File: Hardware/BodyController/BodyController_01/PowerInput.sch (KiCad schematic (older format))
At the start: 39 parts, among them Q1 NX1029X,115, Q2 NX1029X,115, Q4 SQJ423EP-T1_GE3, U14 OPA320-Q1, U2 LM2903QDRQ1, U3 INA21x

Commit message: New bring-up code for Body Controller
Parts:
- C16, C17, C18, C20, C21, C79: MPN CGA4J3X7R1H105K125AE -> CGA4J3X7R1H105M125AE
- D8: MPN MMSZ4702T1G -> MMSZ5245BT1G
- R14, R15: value 10R -> 3R0; MPN AC0603FR-0710RL -> ERJ-3GEYJ3R0V
- U2: MPN LM2903QDRQ1 -> LM2903AVQPWRG4Q1
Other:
- note added: "27A efuse\n20A/V\nOffset at 1.65V"
- note added: "Gain: 100V/V"
- note removed: "71A efuse\n25A/V\nOffset at 1.65V"
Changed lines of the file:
@@
-$EndComp
-$Comp
-L R R14
-U 1 1 599A2E3C
-P 6850 4550
-F 0 "R14" V 6930 4550 50  0000 C CNN
-F 1 "10R" V 6850 4550 50  0000 C CNN
-F 2 "Resistors_SMD:R_0603" V 6780 4550 50  0001 C CNN
-F 3 "http://www.yageo.com/NewPortal/yageodocoutput?fileName=/pdf/R-Chip/PYu-AC_51_RoHS_L_6.pdf" H 6850 4550 50  0001 C CNN
-F 4 "AC0603FR-0710RL" H 6930 4650 50  0001 C CNN "MPN"
-F 5 "y" H 6930 4650 50  0001 C CNN "populate"
-	1    6850 4550
-	0    1    1    0
-$EndComp
-$Comp
-L R R15
-U 1 1 599A2EC8
-P 6850 4950
-F 0 "R15" V 6930 4950 50  0000 C CNN
-F 1 "10R" V 6850 4950 50  0000 C CNN
-F 2 "Resistors_SMD:R_0603" V 6780 4950 50  0001 C CNN
-F 3 "http://www.yageo.com/NewPortal/yageodocoutput?fileName=/pdf/R-Chip/PYu-AC_51_RoHS_L_6.pdf" H 6850 4950 50  0001 C CNN
-F 4 "AC0603FR-0710RL" H 6930 5050 50  0001 C CNN "MPN"
-F 5 "y" H 6930 5050 50  0001 C CNN "populate"
-	1    6850 4950
-	0    1    1    0
 $EndComp
 $Comp
@@
 F 1 "1uF" H 6675 4250 50  0000 L CNN
 F 2 "Capacitors_SMD:C_0805" H 6688 4200 50  0001 C CNN
-F 3 "https://product.tdk.com/info/en/documents/chara_sheet/CGA4J3X7R1H105K125AE.pdf" H 6650 4350 50  0001 C CNN
-F 4 "CGA4J3X7R1H105K125AE" H 6675 4550 50  0001 C CNN "MPN"
+F 3 "https://product.tdk.com/info/en/documents/chara_sheet/CGA4J3X7R1H105M125AE.pdf" H 6650 4350 50  0001 C CNN
+F 4 "CGA4J3X7R1H105M125AE" H 6675 4550 50  0001 C CNN "MPN"
 F 5 "y" H 6675 4550 50  0001 C CNN "populate"
 	1    6650 4350
@@
 L GND #PWR023
 U 1 1 599A3E31
-P 6650 5350
-F 0 "#PWR023" H 6650 5100 50  0001 C CNN
-F 1 "GND" H 6650 5200 50  0000 C CNN
-F 2 "" H 6650 5350 50  0001 C CNN
-F 3 "" H 6650 5350 50  0001 C CNN
-	1    6650 5350
+P 6650 5450
+F 0 "#PWR023" H 6650 5200 50  0001 C CNN
+F 1 "GND" H 6650 5300 50  0000 C CNN
+F 2 "" H 6650 5450 50  0001 C CNN
+F 3 "" H 6650 5450 50  0001 C CNN
+	1    6650 5450
 	1    0    0    -1
 $EndComp
@@
 L C C18
 U 1 1 599A3E37
-P 6650 5150
-F 0 "C18" H 6675 5250 50  0000 L CNN
-F 1 "1uF" H 6675 5050 50  0000 L CNN
-F 2 "Capacitors_SMD:C_0805" H 6688 5000 50  0001 C CNN
-F 3 "https://product.tdk.com/info/en/documents/chara_sheet/CGA4J3X7R1H105K125AE.pdf" H 6650 5150 50  0001 C CNN
-F 4 "CGA4J3X7R1H105K125AE" H 6675 5350 50  0001 C CNN "MPN"
-F 5 "y" H 6675 5350 50  0001 C CNN "populate"
-	1    6650 5150
+P 6650 5250
+F 0 "C18" H 6675 5350 50  0000 L CNN
+F 1 "1uF" H 6675 5150 50  0000 L CNN
+F 2 "Capacitors_SMD:C_0805" H 6688 5100 50  0001 C CNN
+F 3 "https://product.tdk.com/info/en/documents/chara_sheet/CGA4J3X7R1H105M125AE.pdf" H 6650 5250 50  0001 C CNN
+F 4 "CGA4J3X7R1H105M125AE" H 6675 5450 50  0001 C CNN "MPN"
+F 5 "y" H 6675 5450 50  0001 C CNN "populate"
+	1    6650 5250
 	1    0    0    -1
 $EndComp
@@
 F 1 "1uF" H 6575 4650 50  0000 L CNN
 F 2 "Capacitors_SMD:C_0805" H 6588 4600 50  0001 C CNN
-F 3 "https://product.tdk.com/info/en/documents/chara_sheet/CGA4J3X7R1H105K125AE.pdf" H 6550 4750 50  0001 C CNN
-F 4 "CGA4J3X7R1H105K125AE" H 6575 4950 50  0001 C CNN "MPN"
+F 3 "https://product.tdk.com/info/en/documents/chara_sheet/CGA4J3X7R1H105M125AE.pdf" H 6550 4750 50  0001 C CNN
+F 4 "CGA4J3X7R1H105M125AE" H 6575 4950 50  0001 C CNN "MPN"
 F 5 "y" H 6575 4950 50  0001 C CNN "populate"
 	1    6550 4750
@@
 F 1 "1uF" H 10275 5800 50  0000 L CNN
 F 2 "Capacitors_SMD:C_0805" H 10288 5750 50  0001 C CNN
-F 3 "https://product.tdk.com/info/en/documents/chara_sheet/CGA4J3X7R1H105K125AE.pdf" H 10250 5900 50  0001 C CNN
-F 4 "CGA4J3X7R1H105K125AE" H 10275 6100 50  0001 C CNN "MPN"
+F 3 "https://product.tdk.com/info/en/documents/chara_sheet/CGA4J3X7R1H105M125AE.pdf" H 10250 5900 50  0001 C CNN
+F 4 "CGA4J3X7R1H105M125AE" H 10275 6100 50  0001 C CNN "MPN"
 F 5 "y" H 10275 6100 50  0001 C CNN "populate"
 	1    10250 5900
@@
 F 2 "Footprints:TSSOP-8_3x4.4mm_Pitch0.65mm" H 4400 4600 39  0001 C CNN
 F 3 "http://www.ti.com/lit/ds/symlink/lm2903-q1.pdf" H 4400 4600 39  0001 C CNN
-F 4 "LM2903QDRQ1" H 3400 5150 50  0001 C CNN "MPN"
+F 4 "LM2903AVQPWRG4Q1 " H 3400 5150 50  0001 C CNN "MPN"
 F 5 "y" H 3400 5150 50  0001 C CNN "populate"
 	1    3700 4850
@@
 F 2 "Footprints:TSSOP-8_3x4.4mm_Pitch0.65mm" H 3850 6300 39  0001 C CNN
 F 3 "http://www.ti.com/lit/ds/symlink/lm2903-q1.pdf" H 3850 6300 39  0001 C CNN
-F 4 "LM2903QDRQ1" H 2850 6850 50  0001 C CNN "MPN"
+F 4 "LM2903AVQPWRG4Q1 " H 2850 6850 50  0001 C CNN "MPN"
 F 5 "y" H 2850 6850 50  0001 C CNN "populate"
 	2    3150 6550
@@
 F 1 "D_Zener_15V" H 5150 1450 50  0000 C CNN
 F 2 "Diodes_SMD:D_SOD-123" H 5150 1550 50  0001 C CNN
-F 3 "http://www.onsemi.com/pub/Collateral/MMSZ4678T1-D.PDF" H 5150 1550 50  0001 C CNN
-F 4 "MMSZ4702T1G" H 5150 1750 50  0001 C CNN "MPN"
+F 3 "http://www.onsemi.com/pub/Collateral/MMSZ5221BT1-D.PDF" H 5150 1550 50  0001 C CNN
+F 4 "MMSZ5245BT1G" H 5150 1750 50  0001 C CNN "MPN"
 F 5 "y" H 5150 1750 50  0001 C CNN "populate"
 	1    5150 1550
@@
 F 1 "1uF" H 9425 5800 50  0000 L CNN
 F 2 "Capacitors_SMD:C_0805" H 9438 5750 50  0001 C CNN
-F 3 "https://product.tdk.com/info/en/documents/chara_sheet/CGA4J3X7R1H105K125AE.pdf" H 9400 5900 50  0001 C CNN
-F 4 "CGA4J3X7R1H105K125AE" H 9425 6100 50  0001 C CNN "MPN"
+F 3 "https://product.tdk.com/info/en/documents/chara_sheet/CGA4J3X7R1H105M125AE.pdf" H 9400 5900 50  0001 C CNN
+F 4 "CGA4J3X7R1H105M125AE" H 9425 6100 50  0001 C CNN "MPN"
 F 5 "y" H 9425 6100 50  0001 C CNN "populate"
 	1    9400 5900
@@
 F 1 "1uF" H 8375 5800 50  0000 L CNN
 F 2 "Capacitors_SMD:C_0805" H 8388 5750 50  0001 C CNN
-F 3 "https://product.tdk.com/info/en/documents/chara_sheet/CGA4J3X7R1H105K125AE.pdf" H 8350 5900 50  0001 C CNN
-F 4 "CGA4J3X7R1H105K125AE" H 8375 6100 50  0001 C CNN "MPN"
+F 3 "https://product.tdk.com/info/en/documents/chara_sheet/CGA4J3X7R1H105M125AE.pdf" H 8350 5900 50  0001 C CNN
+F 4 "CGA4J3X7R1H105M125AE" H 8375 6100 50  0001 C CNN "MPN"
 F 5 "y" H 8375 6100 50  0001 C CNN "populate"
 	1    8350 5900
@@
 	1    0    0    -1
 $EndComp
+$Comp
+L R R14
+U 1 1 5A8741DE
+P 6850 4550
+F 0 "R14" V 6930 4550 50  0000 C CNN
+F 1 "3R0" V 6850 4550 50  0000 C CNN
+F 2 "Resistors_SMD:R_0603" V 6780 4550 50  0001 C CNN
+F 3 "http://industrial.panasonic.com/www-cgi/jvcr13pz.cgi?E+PZ+3+AOA0001+ERJ3GEYJ3R0V+7+WW" H 6850 4550 50  0001 C CNN
+F 4 "ERJ-3GEYJ3R0V" H 6930 4650 50  0001 C CNN "MPN"
+F 5 "y" H 6930 4650 50  0001 C CNN "populate"
+	1    6850 4550
+	0    1    1    0
+$EndComp
+$Comp
+L R R15
+U 1 1 5A874231
+P 6850 4950
+F 0 "R15" V 6930 4950 50  0000 C CNN
+F 1 "3R0" V 6850 4950 50  0000 C CNN
+F 2 "Resistors_SMD:R_0603" V 6780 4950 50  0001 C CNN
+F 3 "http://industrial.panasonic.com/www-cgi/jvcr13pz.cgi?E+PZ+3+AOA0001+ERJ3GEYJ3R0V+7+WW" H 6850 4950 50  0001 C CNN
+F 4 "ERJ-3GEYJ3R0V" H 6930 5050 50  0001 C CNN "MPN"
+F 5 "y" H 6930 5050 50  0001 C CNN "populate"
+	1    6850 4950
+	0    1    1    0
+$EndComp
 Text Notes 6500 6400 2    98   ~ 0
-71A efuse\n25A/V\nOffset at 1.65V
+27A efuse\n20A/V\nOffset at 1.65V
 Text GLabel 4650 3450 0    98   Output ~ 0
 BATT_ISENSE_AI
@@
 Text GLabel 7400 5200 2    60   Output ~ 0
 1V65_REF
+Text Notes 5600 4400 0    60   ~ 0
+Gain: 100V/V
 Wire Wire Line
 	1300 850  1300 1000
@@
 	6650 4200 6650 4150
 Wire Wire Line
-	6650 5350 6650 5300
-Wire Wire Line
-	6650 5000 6650 4950
+	6650 5450 6650 5400
+Wire Wire Line
+	6650 5100 6650 4950
 Wire Wire Line
 	6550 4600 6550 4550
@@
 	8050 5500 8050 5600
 Wire Wire Line
-	8050 6350 8050 6250
+	8050 6250 8050 6350
 Wire Wire Line
 	8350 6050 8350 6300
@@
 	8350 5550 8050 5550
 Wire Wire Line
-	7400 4750 6200 4750
+	6200 4750 7400 4750
 Wire Wire Line
 	7250 4750 7250 5200
@@
 Connection ~ 7250 4750
 Connection ~ 7250 5050
+Connection ~ 2800 4450
 NoConn ~ 3650 6550
-Connection ~ 2800 4450
 $EndSCHEMATC

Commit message: too much work to specify all. New Scheduler, new bootloader, added new Hardware projects, updated code for bringup, COnverted kicad files to new version.
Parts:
- C11, C14, C15, C16, C17, C18, C19, C20, C21, C22, C79: symbol C -> BodyController_01-rescue:C-RESCUE-BodyController_01
- C12, C13: symbol CP -> BodyController_01-rescue:CP-RESCUE-BodyController_01
- D15: symbol D_TVS -> BodyController_01-rescue:D_TVS-RESCUE-BodyController_01
- D8: symbol D_Zener -> BodyController_01-rescue:D_Zener-RESCUE-BodyController_01
- NT1, NT2: symbol Net_Tie-0.5mm -> BodyController_01-rescue:Net_Tie-0.5mm-RESCUE-BodyController_01
- Q1, Q2: symbol NX1029X,115 -> BodyController_01-rescue:NX1029X,115-RESCUE-BodyController_01
- Q4: symbol SQJ423EP-T1_GE3 -> BodyController_01-rescue:SQJ423EP-T1_GE3-RESCUE-BodyController_01
- R10, R111, R113, R12, R13, R14, R15, R16, R17, R18, R2, R5, R6, R7, R8, R9: symbol R -> BodyController_01-rescue:R-RESCUE-BodyController_01
- U14: symbol OPA320-Q1 -> BodyController_01-rescue:OPA320-Q1-RESCUE-BodyController_01
- U2: symbol LM2903QDRQ1 -> BodyController_01-rescue:LM2903QDRQ1-RESCUE-BodyController_01
- U3: symbol INA21x -> BodyController_01-rescue:INA21x-RESCUE-BodyController_01

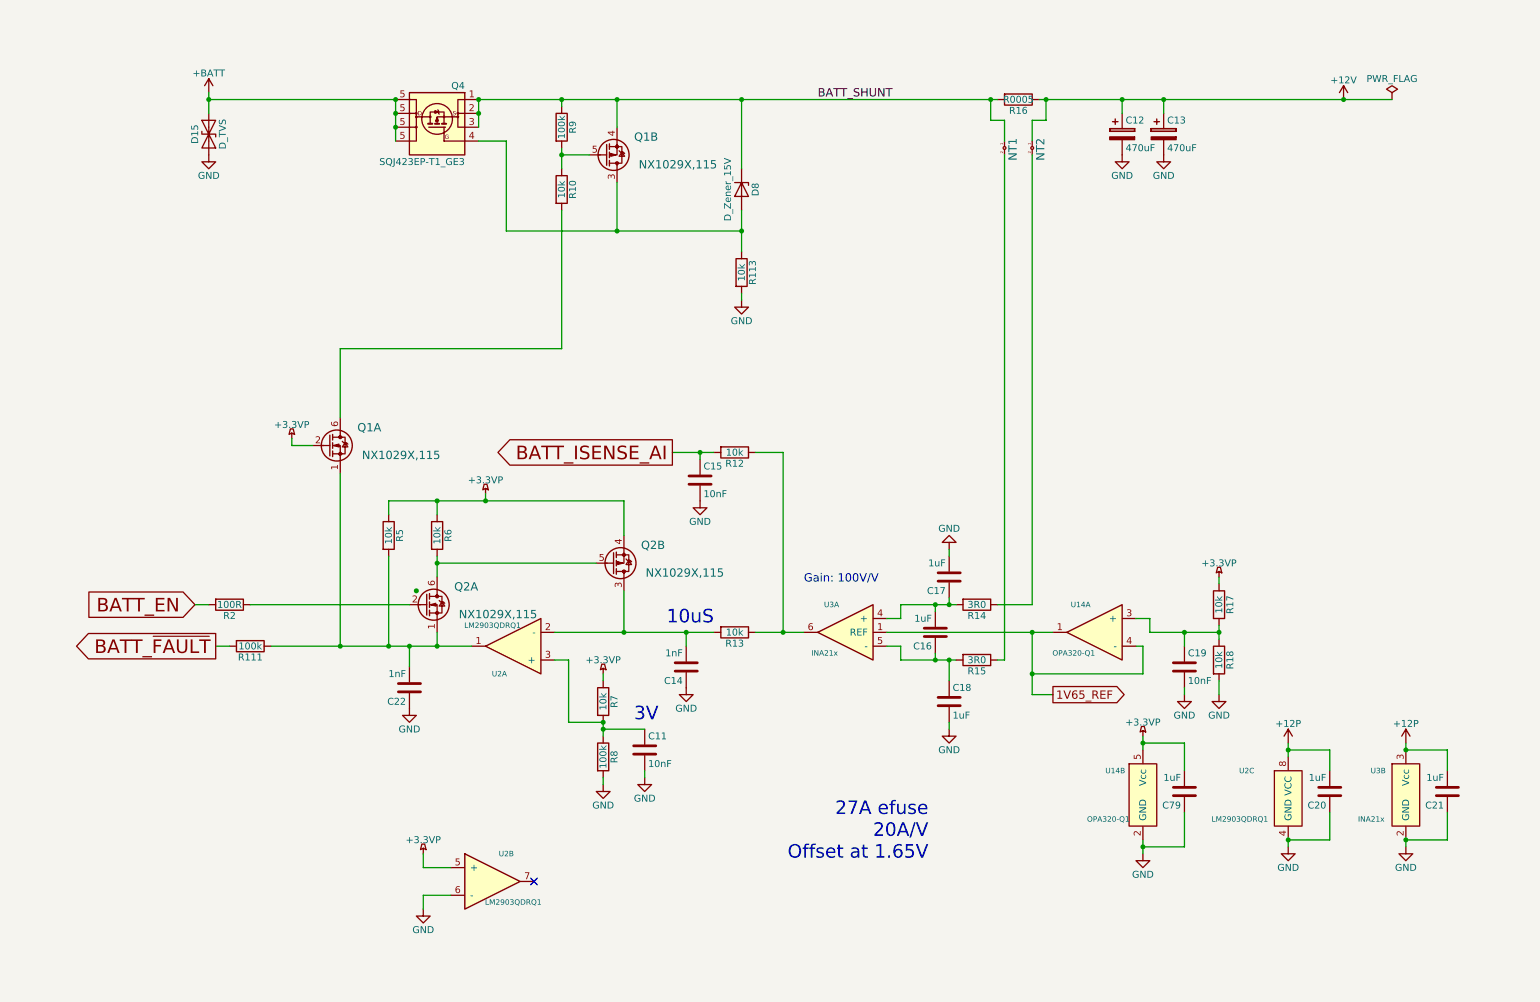
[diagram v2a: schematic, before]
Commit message: changed some directory locations, added new DCDC PBC project, few Body controller light and switches changes
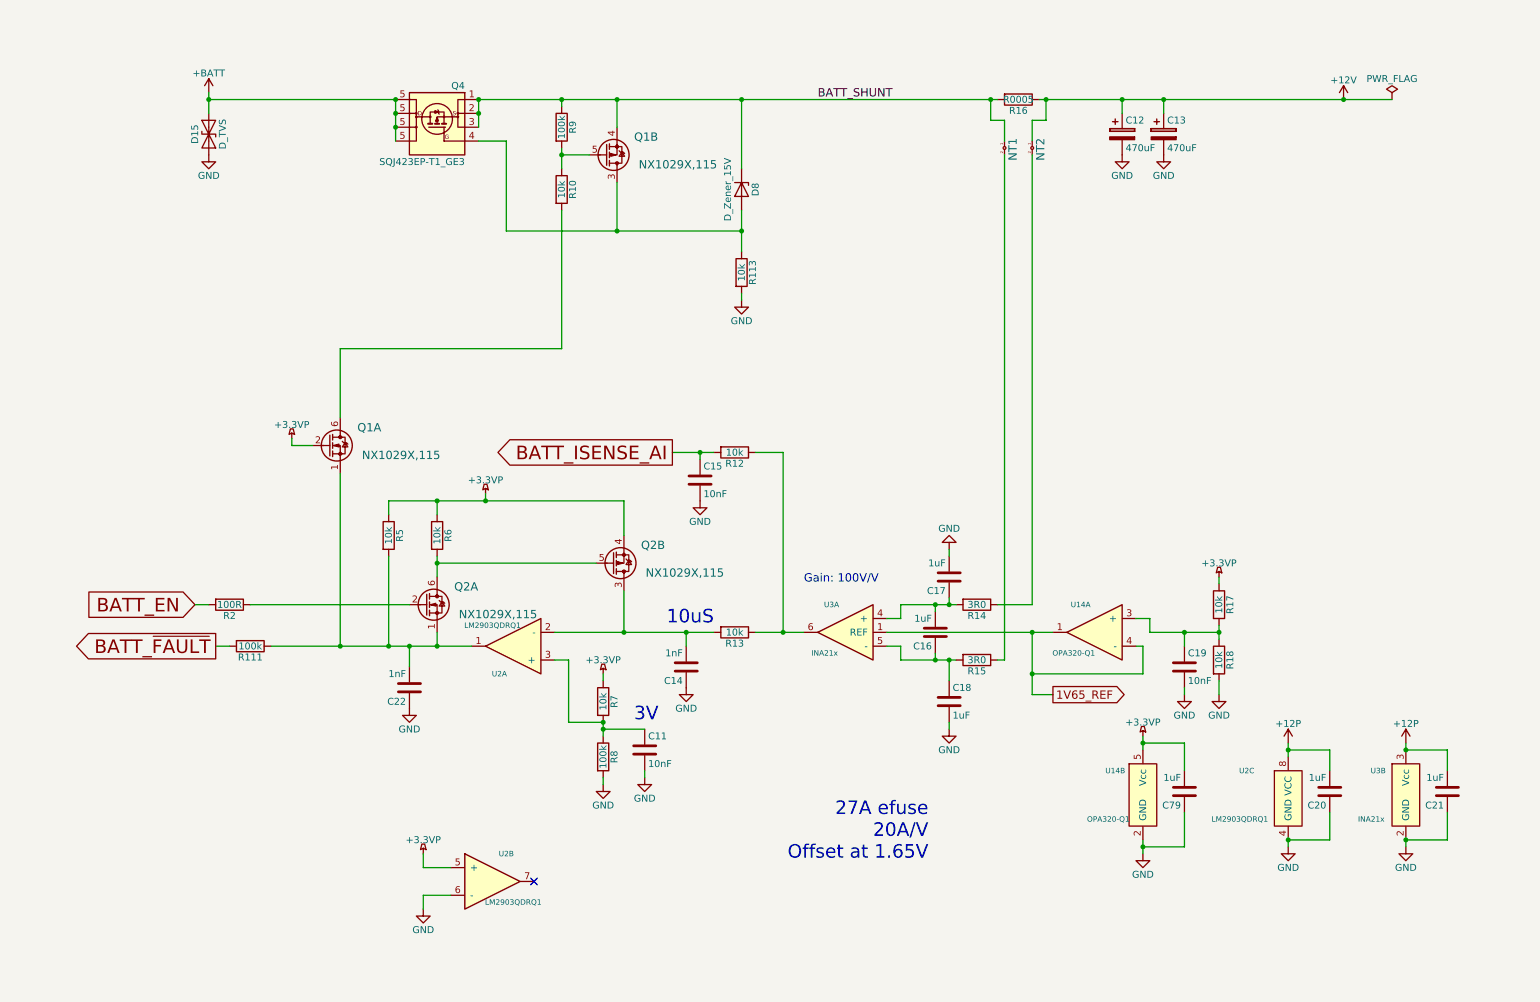
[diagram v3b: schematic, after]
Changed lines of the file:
@@
 Gain: 100V/V
 Wire Wire Line
-	1300 850  1300 1000
-Wire Wire Line
-	7300 900  9850 900
+	1300 850  1300 900
+Wire Wire Line
+	7300 900  7350 900
 Wire Wire Line
 	7900 900  7900 1000
@@
 	7000 4550 7250 4550
 Wire Wire Line
-	6300 4550 6700 4550
-Wire Wire Line
-	6300 4950 6700 4950
+	6300 4550 6550 4550
+Wire Wire Line
+	6300 4950 6550 4950
 Wire Wire Line
 	7050 4950 7000 4950
@@
 	5450 3450 5250 3450
 Wire Wire Line
-	4650 3450 4950 3450
+	4650 3450 4850 3450
 Wire Wire Line
 	4850 3450 4850 3500
 Wire Wire Line
-	5250 4750 5600 4750
-Wire Wire Line
-	3800 4750 4950 4750
+	5250 4750 5450 4750
+Wire Wire Line
+	3800 4750 4300 4750
 Wire Wire Line
 	4750 4850 4750 4750
@@
 	8600 5100 8600 5200
 Wire Wire Line
-	8600 4700 8600 4800
+	8600 4700 8600 4750
 Wire Wire Line
 	8350 5200 8350 5150
@@
 	4150 5850 4150 5800
 Wire Wire Line
-	4150 5400 4150 5500
+	4150 5400 4150 5450
 Wire Wire Line
 	4150 5100 4150 5050
@@
 	9400 5600 9400 5750
 Wire Wire Line
-	1750 4850 3200 4850
+	1750 4850 2250 4850
 Wire Wire Line
 	2950 4750 2950 4850
@@
 	8600 4350 8600 4400
 Wire Wire Line
-	2950 4200 2950 4350
+	2950 4200 2950 4250
 Wire Wire Line
 	2950 4250 4100 4250
@@
 	4300 3800 4300 4050
 Wire Wire Line
-	2600 3800 4300 3800
+	2600 3800 2950 3800
 Wire Wire Line
 	2950 3900 2950 3800
@@
 	3900 4950 3800 4950
 Wire Wire Line
-	9100 5550 9100 5650
+	9100 5550 9100 5600
 Wire Wire Line
 	9100 5600 9400 5600
@@
 	2750 4850 2750 5000
 Wire Wire Line
-	3250 900  7000 900
-Wire Wire Line
-	3450 1850 5150 1850
-Wire Wire Line
-	5150 1700 5150 2000
+	3250 900  3850 900
+Wire Wire Line
+	3450 1850 4250 1850
+Wire Wire Line
+	5150 1700 5150 1850
 Wire Wire Line
 	4250 1850 4250 1500
@@
 	4050 1300 3850 1300
 Wire Wire Line
-	3850 1250 3850 1400
+	3850 1250 3850 1300
 Wire Wire Line
 	3850 950  3850 900
@@
 	3450 1200 3250 1200
 Wire Wire Line
-	3250 900  3250 1100
-Wire Wire Line
-	2650 900  2650 1200
+	3250 900  3250 1000
+Wire Wire Line
+	2650 900  2650 1000
 Wire Wire Line
 	7050 1050 6950 1050
@@
 	2850 6650 2850 6750
 Wire Wire Line
-	8100 4750 8600 4750
-Wire Wire Line
-	8050 5500 8050 5600
-Wire Wire Line
-	8050 6250 8050 6350
+	8100 4750 8350 4750
+Wire Wire Line
+	8050 5500 8050 5550
+Wire Wire Line
+	8050 6250 8050 6300
 Wire Wire Line
 	8350 6050 8350 6300
@@
 	8350 5550 8050 5550
 Wire Wire Line
-	6200 4750 7400 4750
-Wire Wire Line
-	7250 4750 7250 5200
+	6200 4750 7250 4750
+Wire Wire Line
+	7250 4750 7250 5050
 Wire Wire Line
 	7250 5050 8050 5050
@@
 Connection ~ 7250 4750
 Connection ~ 7250 5050
-Connection ~ 2800 4450
 NoConn ~ 3650 6550
+Wire Wire Line
+	9500 900  9850 900
+Wire Wire Line
+	8200 900  9500 900
+Wire Wire Line
+	7900 900  8200 900
+Wire Wire Line
+	6650 4550 6700 4550
+Wire Wire Line
+	6650 4950 6700 4950
+Wire Wire Line
+	6550 4550 6650 4550
+Wire Wire Line
+	6550 4950 6650 4950
+Wire Wire Line
+	5450 4750 5600 4750
+Wire Wire Line
+	4850 3450 4950 3450
+Wire Wire Line
+	4750 4750 4950 4750
+Wire Wire Line
+	8600 4750 8600 4800
+Wire Wire Line
+	8350 4750 8600 4750
+Wire Wire Line
+	4150 5450 4150 5500
+Wire Wire Line
+	4300 4750 4750 4750
+Wire Wire Line
+	2950 4250 2950 4350
+Wire Wire Line
+	2950 3800 3300 3800
+Wire Wire Line
+	3300 3800 4300 3800
+Wire Wire Line
+	2950 4850 3200 4850
+Wire Wire Line
+	9100 5600 9100 5650
+Wire Wire Line
+	2600 4850 2750 4850
+Wire Wire Line
+	2250 4850 2600 4850
+Wire Wire Line
+	2750 4850 2950 4850
+Wire Wire Line
+	1300 900  1300 1000
+Wire Wire Line
+	4250 900  5150 900
+Wire Wire Line
+	4250 1850 5150 1850
+Wire Wire Line
+	5150 900  6950 900
+Wire Wire Line
+	3850 900  4250 900
+Wire Wire Line
+	5150 1850 5150 2000
+Wire Wire Line
+	3850 1300 3850 1400
+Wire Wire Line
+	3250 1000 3250 1100
+Wire Wire Line
+	2650 1000 2650 1100
+Wire Wire Line
+	2650 1100 2650 1200
+Wire Wire Line
+	6950 900  7000 900
+Wire Wire Line
+	7350 900  7900 900
+Wire Wire Line
+	8050 6300 8050 6350
+Wire Wire Line
+	8050 5550 8050 5600
+Wire Wire Line
+	7250 4750 7400 4750
+Wire Wire Line
+	7250 5050 7250 5200
 $EndSCHEMATC
